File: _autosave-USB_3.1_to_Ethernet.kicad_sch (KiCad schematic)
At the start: 5 parts, among them J1 RJ45_JK0654219, U1 LAN7801_9JX, U2 93LC56B_SN, U3 KSZ9031RNXCC, Y1 C3E-8.000-18-3030-R

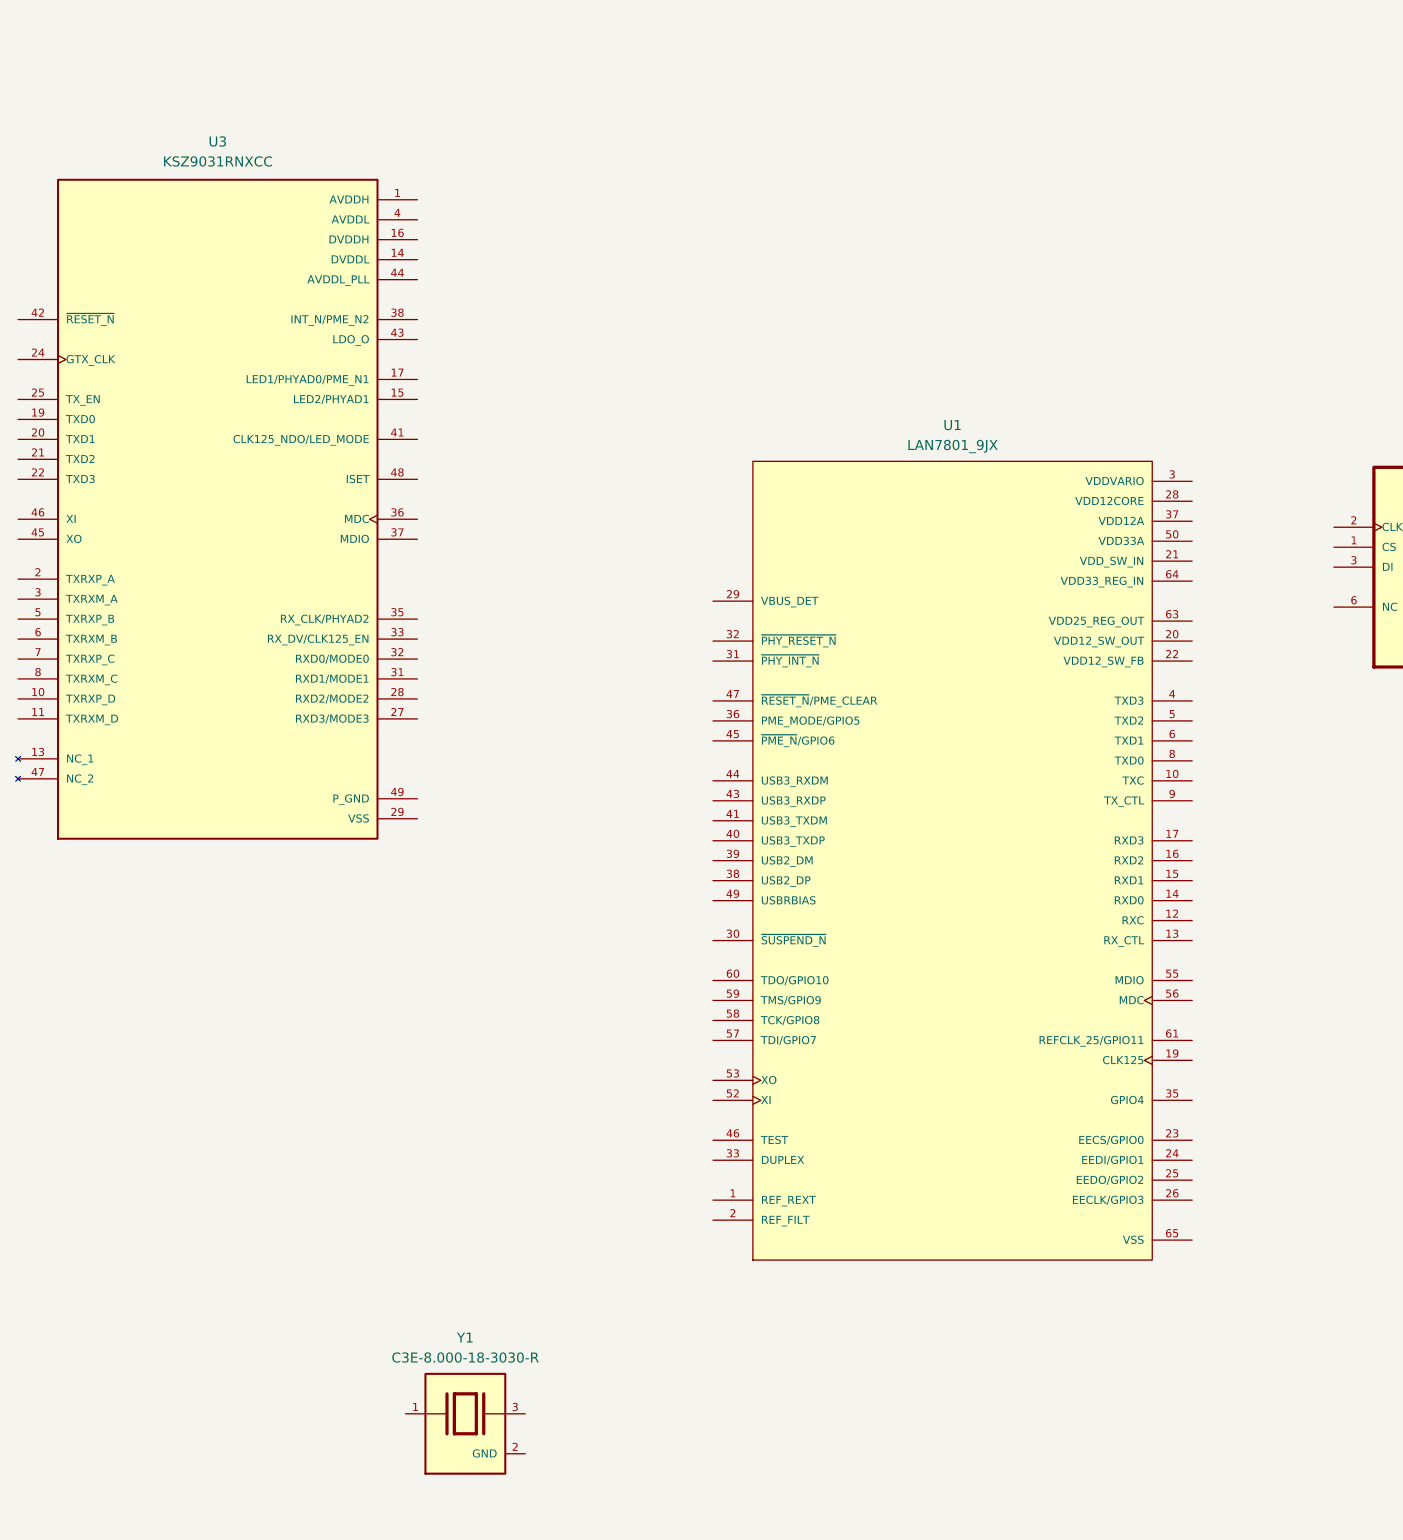
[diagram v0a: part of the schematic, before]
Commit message: power section added and power connections made
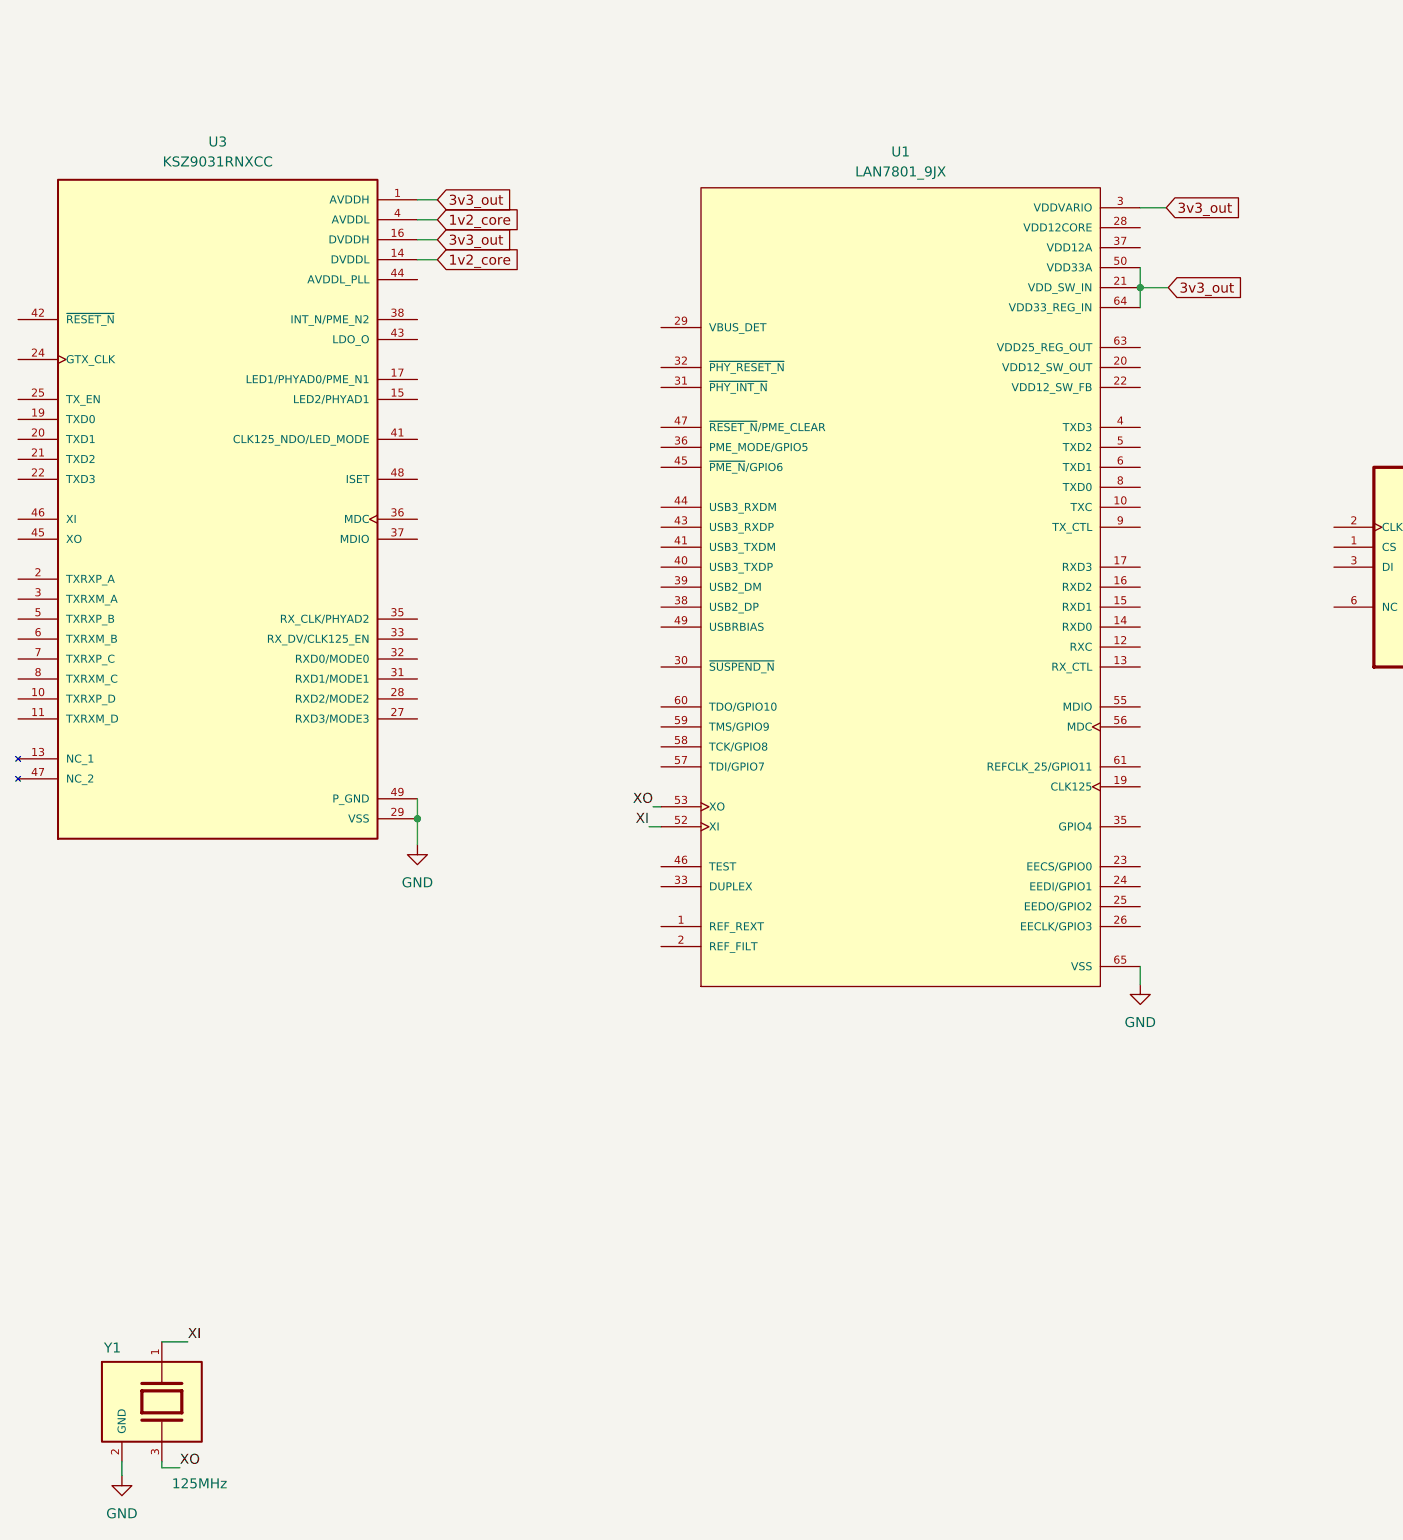
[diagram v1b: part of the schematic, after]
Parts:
- Y1: value C3E-8.000-18-3030-R -> 125MHz
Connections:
- net DVDDH is gone; now on net AVDDH: U3.16 (DVDDH), U3.34 (DVDDH), U3.40 (DVDDH)
- net DVDDL is gone; now on net AVDDL: U3.14 (DVDDL), U3.18 (DVDDL), U3.23 (DVDDL), U3.26 (DVDDL), U3.30 (DVDDL), U3.39 (DVDDL)
- net P_GND is gone; now on net GND: U3.49 (P_GND), U3.49_1 (P_GND), U3.49_10 (P_GND), U3.49_11 (P_GND), U3.49_12 (P_GND), U3.49_13 (P_GND), U3.49_14 (P_GND), U3.49_15 (P_GND), U3.49_16 (P_GND), U3.49_17 (P_GND), U3.49_18 (P_GND), U3.49_19 (P_GND), U3.49_2 (P_GND), U3.49_20 (P_GND), U3.49_21 (P_GND), U3.49_22 (P_GND), U3.49_23 (P_GND), U3.49_24 (P_GND), U3.49_25 (P_GND), U3.49_3 (P_GND), U3.49_4 (P_GND), U3.49_5 (P_GND), U3.49_6 (P_GND), U3.49_7 (P_GND), U3.49_8 (P_GND), U3.49_9 (P_GND)
- net VDDVARIO is gone; now on net AVDDH: U1.11 (VDDVARIO), U1.18 (VDDVARIO), U1.27 (VDDVARIO), U1.3 (VDDVARIO), U1.48 (VDDVARIO), U1.51 (VDDVARIO), U1.7 (VDDVARIO)
- net AVDDH: now also U1.21 (VDD_SW_IN), U1.50 (VDD33A), U1.64 (VDD33_REG_IN)
- net GND: now also U1.65 (VSS), U3.29 (VSS)
- net XI: now reaches Y1.1
- net XI: now also U1.52 (XI)
- net XO: now reaches Y1.3
- net XO: now also U1.53 (XO)
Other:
- moved on the sheet: U1, Y1
